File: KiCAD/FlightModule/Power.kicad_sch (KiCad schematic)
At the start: 14 parts, among them J6 VREF, U3 NJM7805SDL1

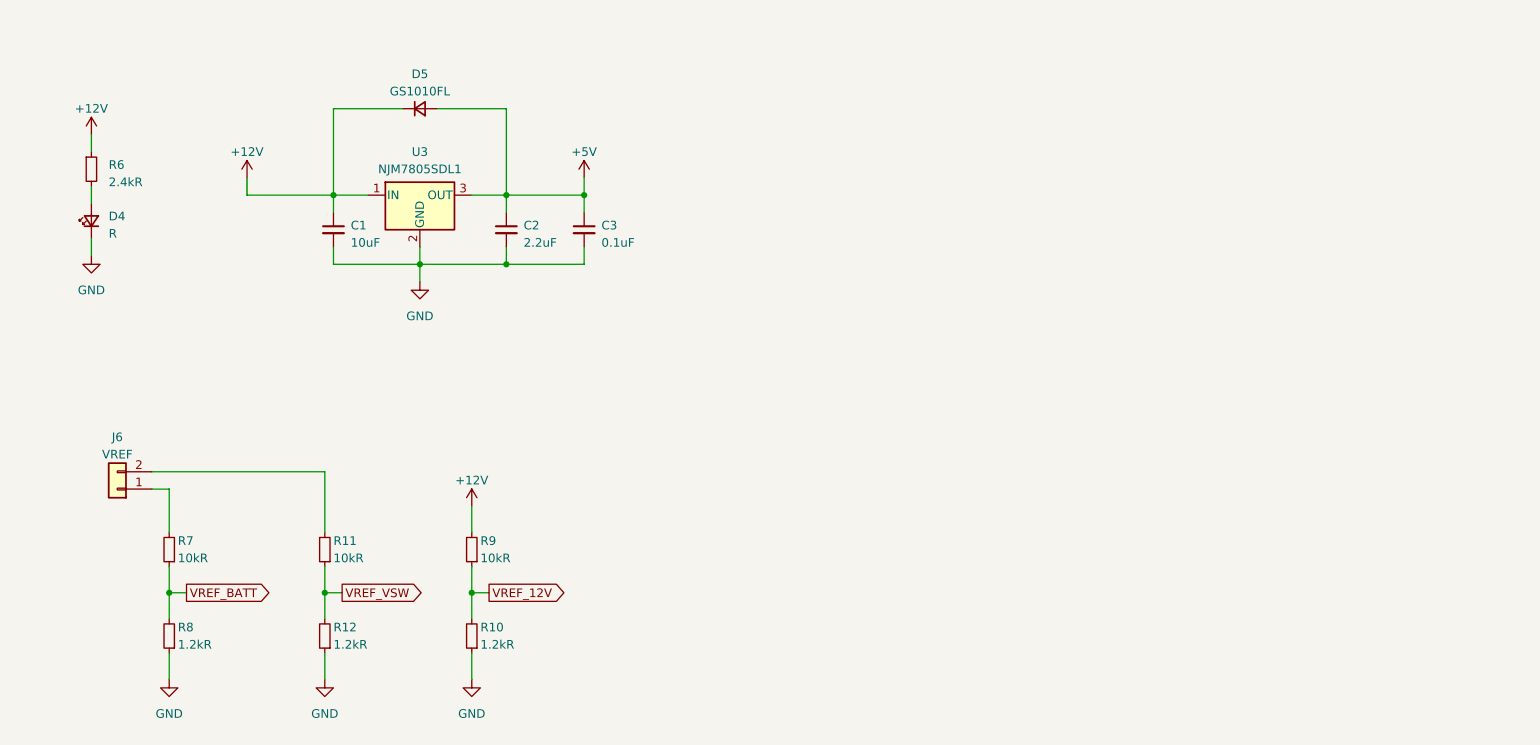
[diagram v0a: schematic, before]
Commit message: DCDCコンバーターを交換，3.3Vレギュレーターを配置
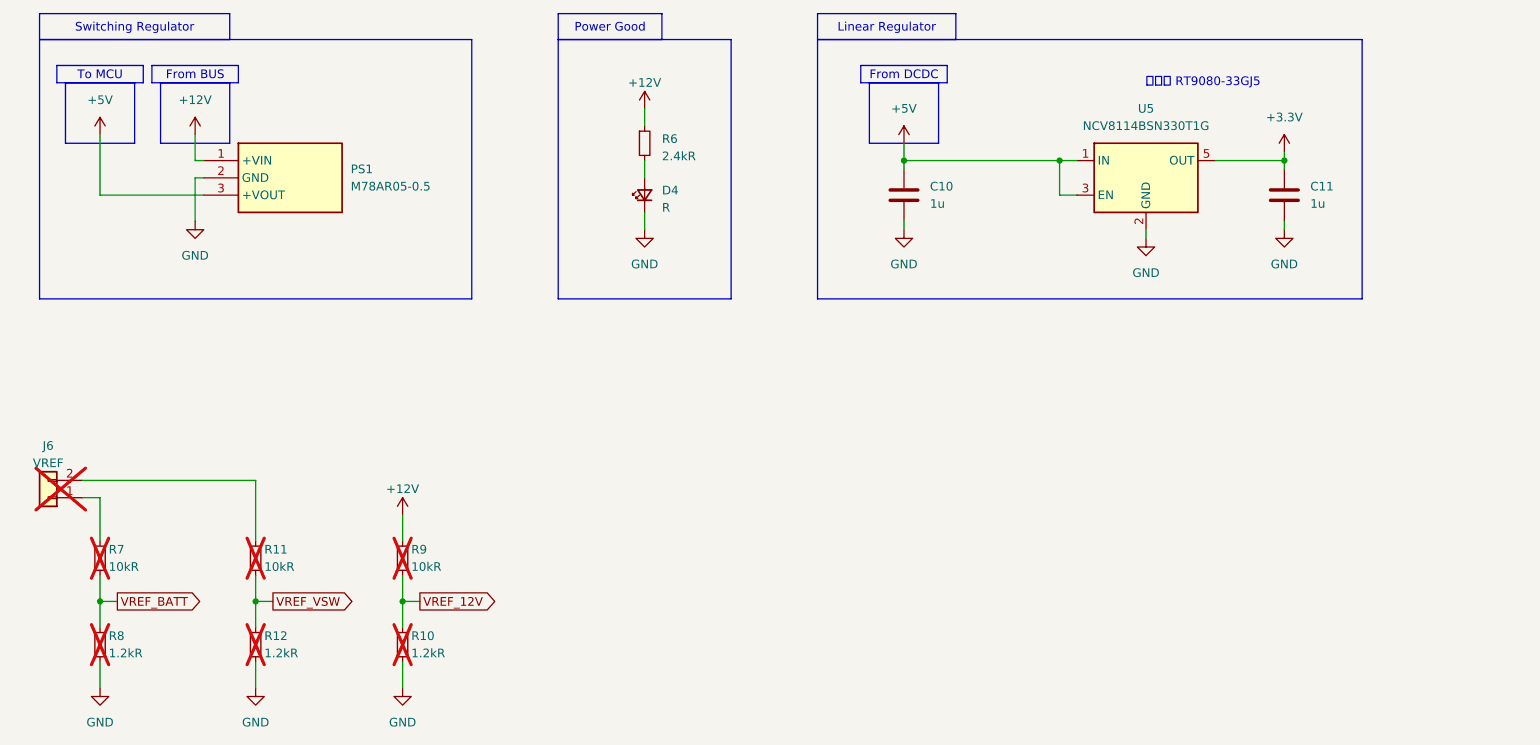
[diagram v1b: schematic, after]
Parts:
- removed C1: 10uF, Capacitor_SMD:C_1206_3216Metric_Pad1.33x1.80mm_HandSolder, symbol Device:C_Small
- removed C2: 2.2uF, Capacitor_SMD:C_0603_1608Metric_Pad1.08x0.95mm_HandSolder, symbol Device:C_Small
- removed C3: 0.1uF, Capacitor_SMD:C_0603_1608Metric_Pad1.08x0.95mm_HandSolder, symbol Device:C_Small
- removed D5: GS1010FL, Diode_SMD:D_SOD-123F, symbol Device:D_Small
- removed U3: NJM7805SDL1, Package_TO_SOT_SMD:TO-252-2, symbol Regulator_Linear:L7805
- added C10, C11: 1u, Capacitor_SMD:C_0603_1608Metric_Pad1.08x0.95mm_HandSolder, symbol Device:C
- added PS1: M78AR05-0.5, TSRP_IC:M78AR03305, symbol TSRP_IC:M78AR05-0.5
- added U5: NCV8114BSN330T1G, Package_TO_SOT_SMD:TSOT-23-5, symbol Regulator_Linear:NCV8114BSN330T1G
- J6, R10, R11, R12, R7, R8, R9: now not fitted; now left out of the parts list
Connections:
- net +12V: now also PS1.1 (+VIN)
- net +5V: now also C10.1, PS1.3 (+VOUT), U5.1 (IN), U5.3 (EN)
- net GND: now also C10.2, C11.2, PS1.2 (GND), U5.2 (GND)
- new net +3.3V: C11.1, U5.5 (OUT)
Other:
- note added: "本当は RT9080-33GJ5"
- moved on the sheet: D4, R6

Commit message: 配線8割り終わり．次の作業....
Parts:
- removed J6: VREF, Hirose_Connector:Hirose_DF1B, symbol Connector_Generic:Conn_01x02
- removed R10, R12, R8: 1.2kR, Resistor_SMD:R_0603_1608Metric_Pad0.98x0.95mm_HandSolder, symbol Device:R_Small
- removed R11, R7, R9: 10kR, Resistor_SMD:R_0603_1608Metric_Pad0.98x0.95mm_HandSolder, symbol Device:R_Small

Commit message: 最終確認終わり
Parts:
- added C1: 330uF, Capacitor_SMD:CP_Elec_10x10, symbol Device:C
- added D5: GS1010FL, Diode_SMD:D_SOD-123F, symbol Device:D
- C10, C11: value 1u -> 1uF; footprint Capacitor_SMD:C_0603_1608Metric_Pad1.08x0.95mm_HandSolder -> Capacitor_SMD:C_0805_2012Metric_Pad1.18x1.45mm_HandSolder
- D4: value R -> Green
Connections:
- net +12V: now also C1.2, D5.2 (A); no longer PS1.1 (+VIN)
- net GND: now also C1.1
- new net: D5.1 (K), PS1.1 (+VIN)
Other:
- moved on the sheet: C10, C11, D4, PS1, R6, U5

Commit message: Build-2完成．今回は発注しない．
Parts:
- C1: symbol Device:C -> Device:C_Polarized
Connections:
- net +12V: now also C1.1; no longer C1.2
- net GND: now also C1.2; no longer C1.1
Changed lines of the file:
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@@
 	)
 	(symbol
-		(lib_id "Device:C")
-		(at 44.45 67.31 180)
+		(lib_id "Device:C_Polarized")
+		(at 44.45 67.31 0)
 		(unit 1)
 		(exclude_from_sim no)
@@
 		(fields_autoplaced yes)
 		(property "Reference" "C1"
-			(at 48.26 66.0399 0)
+			(at 48.26 65.1509 0)
 			(effects
 				(font
 					(size 1.27 1.27)
 				)
-				(justify right)
+				(justify left)
 			)
 		)
 		(property "Value" "330uF"
-			(at 48.26 68.5799 0)
+			(at 48.26 67.6909 0)
 			(effects
 				(font
 					(size 1.27 1.27)
 				)
-				(justify right)
+				(justify left)
 			)
 		)
 		(property "Footprint" "Capacitor_SMD:CP_Elec_10x10"
-			(at 43.4848 63.5 0)
+			(at 45.4152 71.12 0)
 			(effects
 				(font
@@
 			)
 		)
-		(property "Datasheet" "https://akizukidenshi.com/catalog/g/g114450/"
+		(property "Datasheet" "~"
 			(at 44.45 67.31 0)
 			(effects
@@
 			)
 		)
-		(property "Description" "Unpolarized capacitor"
+		(property "Description" "Polarized capacitor"
 			(at 44.45 67.31 0)
 			(effects
